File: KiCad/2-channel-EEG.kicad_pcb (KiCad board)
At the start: 4 copper layers, 90.4 x 55.9 mm, 79 parts, among them J1 Power_Input, J10 ADC_Data, J11 ISO_IN_C, J12 CH1_AVG_EN, J13 MCU_Data, J14 CH2_AVG_EN, J2 Nucleo_3.3, J3 Electrode_Input, J4 GND_select, J5 CH1_REF_Sel, J6 CH2_REF_Sel, J7 Conn_02x01, J8 Conn_02x01, J9 ADC_23, SW1 SW_Push_SPDT, U1 PESE1-S5-S5-M-TR, U10 AD8606, U11 ISO6763-Q1, U2 AD8237, U3 AD8237, U4 AD8606, U5 AD8606, U6 TCR2EF33, U7 AD8606, U8 AD8606, U9 MCP3562R

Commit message: PCB updates
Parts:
- removed J5: CH1_REF_Sel, Connector_PinHeader_2.54mm:PinHeader_2x02_P2.54mm_Vertical
- removed J6: CH2_REF_Sel, Connector_PinHeader_2.54mm:PinHeader_2x02_P2.54mm_Vertical
- U9: footprint Package_QFP:TQFP-52-1EP_10x10mm_P0.65mm_EP6.5x6.5mm -> Package_SO:TSSOP-20_4.4x6.5mm_P0.65mm
- moved J10 186.1 mm to (195.6, 102.6), turned to -90 degrees
- moved C19 179.7 mm to (186.7, 114.0), turned to -90 degrees
- moved C23 173.8 mm to (186.7, 107.7), turned to -90 degrees
- moved J9 169.2 mm to (200.4, 113.8), turned to 90 degrees
- moved U9 167.4 mm to (191.9, 112.0), turned to 90 degrees
- moved C24 165.4 mm to (184.4, 91.0), turned to 90 degrees
- moved C25 160.8 mm to (184.4, 82.8), turned to -90 degrees
- moved J13 160.2 mm to (179.6, 82.8), turned to -90 degrees
- moved J11 156.0 mm to (200.4, 102.6)
- moved J8 155.6 mm to (182.9, 114.3), turned to -90 degrees
- moved J7 154.6 mm to (182.9, 107.4), turned to -90 degrees
- moved C12 150.1 mm to (162.8, 86.6), turned to -90 degrees
- moved U11 147.8 mm to (191.3, 86.9), turned to 90 degrees
- moved C4 146.5 mm to (147.7, 98.6), turned to 90 degrees
- moved R11 136.8 mm to (162.6, 94.7), turned to -90 degrees
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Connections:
- C25 pad 1: +3.3V -> +3.3V_nucleo
- C4 pad 2: +3.3V -> +5V_iso
- C6 pad 1: /REF1_INT -> Net-(U2-VREF)
- C7 pad 1: /REF2_INT -> Net-(U3-VREF)
- C9 pad 2: +3.3V -> +5V_iso
- J10 pad 1: /ADC_SDO -> /ADC_~{CS}
- J10 pad 2: /ADC_SDI -> /ADC_SCK
- J10 pad 3: /ADC_SCK -> /ADC_SDI
- J10 pad 4: /ADC_~{CS} -> /ADC_SDO
- J10 pad 5: /ADC_MCLK -> /ADC_~{IRQ}
- J10 pad 6: /ADC_~{IRQ} -> /ADC_MCLK
- J2 pad 1: +3.3V -> +3.3V_nucleo
- J3 pad 1: /CH2+ -> /CH2-
- J3 pad 2: /CH2- -> /CH2+
- RN1 pad 3: /CH1- -> /CH1+
- RN1 pad 4: /CH1+ -> /CH1-
- RN2 pad 3: /CH2- -> /CH2+
- RN2 pad 4: /CH2+ -> /CH2-
- SW1 pad 1: +3.3V -> +5V_iso
- U1 pad 5: +3.3V -> +5V_iso
- U11 pad 16: +3.3V -> +3.3V_nucleo
- U2 pad 6: /CH1_REF -> Net-(U2-VREF)
- U3 pad 6: /CH2_REF -> Net-(U3-VREF)
- U4 pad 1: /REF1_INT -> Net-(U2-VREF)
- U5 pad 1: /REF2_INT -> Net-(U3-VREF)
- U6 pad 1: +3.3V -> +5V_iso
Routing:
- net +5V_iso: track 0.00 -> 24.2 mm
- net /ADC_SDO: track 0.00 -> 24.2 mm
- net GND1: track 0.00 -> 23.8 mm
- net /ADC_~{IRQ}: track 0.00 -> 21.9 mm
- net /ADC_~{CS}: track 0.00 -> 19.0 mm
- net /ADC_SDI: track 0.00 -> 18.9 mm
- net +3.3V: track 33.0 -> 51.7 mm, vias 13 -> 17
- net /ADC_SCK: track 0.00 -> 17.8 mm
- net GND: track 24.0 -> 40.2 mm, vias 15 -> 26
- net Net-(J12-Pin_1): track 0.00 -> 12.1 mm
- net +5V: track 0.00 -> 11.9 mm
- net /REF2_INT: track 11.3 -> 0.00 mm
- net /REF1_INT: track 11.2 -> 0.00 mm
- net /ADC0: track 0.00 -> 11.1 mm
- net Net-(U10A--): track 0.00 -> 11.1 mm
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- removed copper zone on F.Cu, net +3.3V
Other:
- board size 90.4 x 55.9 mm -> 270.1 x 148.1 mm
- board text added: "+"
- board text added: "+3.3V_NUCLEO"
- board text added: "-"
- board text added: "2-Channel EEG"
- board text added: "5V_in"
- board text added: "ADC2"
- board text added: "ADC3"
- board text added: "ADC_MCLK"
- board text added: "ADC_SCK"
- board text added: "ADC_SDI"
- board text added: "ADC_SDO"
- board text added: "ADC_~{CS}"
- board text added: "ADC_~{IRQ}"
- board text added: "CH1"
- board text added: "CH1+"
- board text added: "CH1-"
- board text added: "CH1_CM"
- board text added: "CH1_GAIN"
- board text added: "CH2"
- board text added: "CH2+"
- board text added: "CH2-"
- board text added: "CH2_CM"
- board text added: "CH2_GAIN"
- board text added: "CH_GND"
- board text added: "ISO_INC"
- board text added: "ISO_OUTC"
- board text added: "MCU_SCK"
- board text added: "MCU_SDI"
- board text added: "MCU_SDO"
- board text added: "MCU_~{CS}"
- board text added: "MCU_~{IRQ}"
- board text added: "OFF"
- board text added: "ON"
- board text added: "T.E"

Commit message: drl filter, additional caps for adc, Rs for adc spi.
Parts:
- removed the R20 at (143.0, 119.9)
- added C19: 10u, Capacitor_SMD:C_0805_2012Metric_Pad1.18x1.45mm_HandSolder, F.Cu at (192.5, 120.4)
- added C25: 10u, Capacitor_SMD:C_0805_2012Metric_Pad1.18x1.45mm_HandSolder, F.Cu at (186.4, 112.0)
- added C27: 1u, Capacitor_SMD:C_0805_2012Metric_Pad1.18x1.45mm_HandSolder, F.Cu at (166.3, 141.5)
- added R23: 10, Resistor_SMD:R_0805_2012Metric_Pad1.20x1.40mm_HandSolder, F.Cu at (186.2, 107.2)
- added R24: 10, Resistor_SMD:R_0805_2012Metric_Pad1.20x1.40mm_HandSolder, F.Cu at (188.5, 107.2)
- added R25: 10, Resistor_SMD:R_0805_2012Metric_Pad1.20x1.40mm_HandSolder, F.Cu at (190.8, 107.2)
- added R26: 10, Resistor_SMD:R_0805_2012Metric_Pad1.20x1.40mm_HandSolder, F.Cu at (193.0, 107.2)
- added R27: 10, Resistor_SMD:R_0805_2012Metric_Pad1.20x1.40mm_HandSolder, F.Cu at (195.3, 107.2)
- added R28: 10, Resistor_SMD:R_0805_2012Metric_Pad1.20x1.40mm_HandSolder, F.Cu at (197.6, 107.2)
- added R29: 1M, Resistor_SMD:R_0805_2012Metric_Pad1.20x1.40mm_HandSolder, F.Cu at (161.6, 144.2)
- C17: value C -> 10u
- C18: value 2u -> 10u
- C20: value 1u -> 10u
- R18: value R -> 100
- moved C20 38.8 mm to (186.4, 116.1), turned to -90 degrees
- moved C24 4.77 mm to (188.7, 112.0)
- moved J2 3.26 mm to (203.2, 92.7)
- moved C21 2.87 mm to (188.7, 116.1)
- moved U10 2.62 mm to (193.5, 114.0)
- renumbered C19 to C21, C21 to C22, C22 to C23, C23 to C24, C24 to C26, C25 to C28, J12 to J10, J13 to J11, J14 to J12, J7 to J5, J8 to J6, J9 to J7, J10 to J8, J11 to J9, R21 to R20, R22 to R21, R23 to R22, U9 to U10, U10 to U9
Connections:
- net +3.3V_nucleo renamed +3V3_nucleo
- C20 pad 1: /Driven_GND -> GND
- C20 pad 2: Net-(C20-Pad2) -> +3.3V
- C22 pad 1: Net-(C20-Pad2) -> /Driven_GND
- J10 pad 1: Net-(J12-Pin_1) -> Net-(J10-Pin_1)
- J12 pad 1: Net-(J12-Pin_1) -> Net-(J10-Pin_1)
- R20 pad 1: Net-(C20-Pad2) -> /Driven_GND
- R21 pad 1: Net-(C20-Pad2) -> /Driven_GND
- U10 pad 13: /ADC_~{CS} -> Net-(U10-~{CS})
- U10 pad 14: /ADC_SCK -> Net-(U10-SCK)
- U10 pad 15: /ADC_SDI -> Net-(U10-SDI)
- U10 pad 16: /ADC_SDO -> Net-(U10-SDO)
- U10 pad 17: /ADC_~{IRQ} -> Net-(U10-~{IRQ}/MDAT)
- U10 pad 18: /ADC_MCLK -> Net-(U10-MCLK)
- U10 pad 3: unconnected-(U9-REFIN--Pad3) -> GND
- U10 pad 4: unconnected-(U9-REFIN+/OUT-Pad4) -> Net-(U10-REFIN+/OUT)
- U9 pad 5: Net-(J12-Pin_1) -> Net-(U9B-+)
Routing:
- net Net-(J12-Pin_1): track 12.1 -> 0.00 mm
- net (no net): track 0.00 -> 12.1 mm
- net /ADC0: track 11.1 -> 0.00 mm
- net /ADC_MCLK: track 10.8 -> 0.00 mm
- net /ADC1: track 10.6 -> 0.00 mm
- net /ADC2: track 9.30 -> 0.00 mm
- net /ADC3: track 8.82 -> 0.00 mm
- net Net-(U10-MCLK): track 0.00 -> 7.57 mm
- net Net-(C20-Pad2): track 7.56 -> 0.00 mm
- net /Driven_GND: track 0.00 -> 7.56 mm
- net Net-(U10-~{IRQ}/MDAT): track 0.00 -> 5.78 mm
- net /ADC_~{IRQ}: track 21.9 -> 17.6 mm
- net Net-(U10-SDO): track 0.00 -> 4.26 mm
- net Net-(U10-~{CS}): track 0.00 -> 4.11 mm
- net Net-(U10-SDI): track 0.00 -> 3.34 mm
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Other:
- board size 270.1 x 148.1 mm -> 341.9 x 204 mm
- board text added: "V1.0"

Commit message: updated DRL and pcb
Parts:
- removed the J10 at (141.7, 104.1)
- removed J12: CH2_AVG_EN, Connector_PinHeader_2.54mm:PinHeader_2x01_P2.54mm_Vertical
- removed the R20 at (146.3, 108.2)
- added C26: 0.1u, Capacitor_SMD:C_0805_2012Metric_Pad1.18x1.45mm_HandSolder, F.Cu at (153.9, 107.4)
- added C29: 1u, Capacitor_SMD:C_0805_2012Metric_Pad1.18x1.45mm_HandSolder, F.Cu at (149.8, 111.7)
- added J7: VGND, Connector_PinHeader_2.54mm:PinHeader_1x01_P2.54mm_Vertical, F.Cu at (126.7, 115.8)
- added R22: 10k, Resistor_SMD:R_0805_2012Metric_Pad1.20x1.40mm_HandSolder, F.Cu at (143.8, 106.7)
- added R30: 1M, Resistor_SMD:R_0805_2012Metric_Pad1.20x1.40mm_HandSolder, F.Cu at (145.7, 111.7)
- added U11: AD8606, Package_SO:MSOP-8_3x3mm_P0.65mm, F.Cu at (148.3, 108.4)
- moved R29 45.5 mm to (149.6, 100.3), turned to 90 degrees
- moved C28 45.3 mm to (147.3, 100.3), turned to -90 degrees
- moved R20 12.1 mm to (138.2, 104.6), turned to 90 degrees
- moved C22 10.9 mm to (140.3, 104.6), turned to 90 degrees
- moved J3 10.2 mm to (126.7, 101.3), turned to 0 degrees
- moved R21 9.87 mm to (139.4, 101.3), turned to 0 degrees
- moved C23 9.12 mm to (139.4, 99.3), turned to 0 degrees
- moved J5 7.11 mm to (182.9, 114.6)
- moved U9 6.95 mm to (143.3, 101.3), turned to 90 degrees
- moved J6 6.87 mm to (182.9, 107.4)
- moved J4 6.27 mm to (140.0, 114.3), turned to 180 degrees
- moved J8 2.55 mm to (200.4, 111.2), turned to -90 degrees
- moved RN1 2.32 mm to (148.8, 104.4), turned to 180 degrees
- moved C4 2.05 mm to (149.1, 97.0), turned to 180 degrees
- moved C19 1.63 mm to (193.8, 119.4), turned to 0 degrees
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- renumbered C17 to C16, C18 to C17, C16 to C18, C3 to C2, C26 to C27, C27 to C28, C2 to C3, C28 to C30, C7 to C6, C6 to C7, J9 to J10, J7 to J8, J8 to J9, R3 to R1, R16 to R14, R17 to R15, R14 to R16, R15 to R17, R4 to R2, R21 to R20, R22 to R21, R1 to R3, R2 to R4, R6 to R5, R5 to R6, R8 to R7, R7 to R8, U11 to U12, U3 to U2, U2 to U3, U5 to U4, U4 to U5
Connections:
- C16 pad 2: /CH2_AO -> /CH1_AO
- C17 pad 2: /CH1_AO -> /CH2_AO
- C28 pad 2: Net-(J10-Pin_1) -> Net-(C28-Pad2)
- J3 pad 1: /CH2- -> /CH2+
- J3 pad 2: /CH2+ -> /CH2-
- J3 pad 4: /CH1- -> /CH1+
- J3 pad 5: /CH1+ -> /CH1-
- J4 pad 3: unconnected-(J4-Pin_3-Pad3) -> /VGND
- R18 pad 1: /CH2_AO -> /CH1_AO
- R19 pad 1: /CH1_AO -> /CH2_AO
- RN1 pad 1: Net-(J10-Pin_2) -> Net-(C28-Pad2)
- RN1 pad 2: Net-(J10-Pin_2) -> Net-(C28-Pad2)
- RN1 pad 3: /CH1+ -> /CH2+
- RN1 pad 4: /CH1- -> /CH2-
- RN2 pad 3: /CH2+ -> /CH1+
- RN2 pad 4: /CH2- -> /CH1-
- U2 pad 2: /CH2+ -> /CH1+
- U2 pad 3: /CH2- -> /CH1-
- U3 pad 2: /CH1+ -> /CH2+
- U3 pad 3: /CH1- -> /CH2-
- U9 pad 1: Net-(R20-Pad2) -> /Driven_GND
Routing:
- net /CH2+: track 3.71 -> 27.0 mm
- net /ISO_INC: track 0.18 -> 20.7 mm
- net /ADC1: track 0.00 -> 15.0 mm
- net (no net): track 12.1 -> 0.00 mm
- net /ADC0: track 0.00 -> 11.7 mm
- net /ADC2: track 0.00 -> 8.66 mm
- net /ADC3: track 0.00 -> 6.96 mm
- net Net-(U11A-+): track 0.00 -> 6.14 mm
- net Net-(U9B-+): track 0.00 -> 5.42 mm
- net /ADC_MCLK: track 0.00 -> 4.94 mm
- net Net-(J10-Pin_2): track 4.23 -> 0.00 mm
- net Net-(U9A--): track 11.1 -> 7.12 mm
- net Net-(U11A--): track 0.00 -> 3.22 mm
- net Net-(C28-Pad2): track 0.00 -> 2.80 mm
- net GND: track 40.4 -> 37.7 mm, vias 23 -> 21
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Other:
- board text removed: "CH1_CM"
- board text removed: "CH2_CM"
- board text removed: "CH2_GAIN"

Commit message: added solder jumpers between INA and filter
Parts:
- added JP1: SolderJumper_2_Open, Resistor_SMD:R_0603_1608Metric, F.Cu at (158.5, 109.3)
- added JP2: SolderJumper_2_Open, Resistor_SMD:R_0603_1608Metric, F.Cu at (158.5, 99.1)
- moved J4 5.36 mm to (137.2, 109.7), turned to 0 degrees
- moved J10 3.78 mm to (203.2, 105.2)
- moved J8 2.79 mm to (203.2, 111.2)
- moved C4 2.15 mm to (147.1, 96.3), turned to 90 degrees
- moved U1 1.90 mm to (141.0, 89.4)
- moved RV2 1.80 mm to (170.2, 95.5)
- moved R11 1.72 mm to (164.1, 94.0), turned to 0 degrees
- moved R21 1.70 mm to (137.9, 100.6), turned to 90 degrees
- moved C23 1.54 mm to (140.3, 100.6), turned to 90 degrees
- moved R7 1.52 mm to (158.5, 107.4)
- moved C19 1.52 mm to (192.3, 119.4), turned to 180 degrees
- moved J3 1.52 mm to (126.7, 99.8)
- moved R8 1.52 mm to (158.5, 97.0)
- moved R17 1.30 mm to (177.5, 99.1)
- moved J11 1.27 mm to (179.6, 84.1)
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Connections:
- R1 pad 1: Net-(R1-Pad1) -> Net-(JP1-A)
- R21 pad 1: Net-(U9A--) -> Net-(U9B--)
- R21 pad 2: Net-(U9B--) -> Net-(U9A--)
- R3 pad 1: Net-(R3-Pad1) -> Net-(JP2-A)
- R5 pad 2: Net-(R1-Pad1) -> Net-(JP1-A)
- R6 pad 2: Net-(R3-Pad1) -> Net-(JP2-A)
- R7 pad 2: Net-(R1-Pad1) -> Net-(JP1-B)
- R8 pad 2: Net-(R3-Pad1) -> Net-(JP2-B)
- U2 pad 8: Net-(R1-Pad1) -> Net-(JP1-A)
- U3 pad 8: Net-(R3-Pad1) -> Net-(JP2-A)
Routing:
- net GND1: track 23.8 -> 88.5 mm, vias 0 -> 2
- net /MCU_~{CS}: track 0.00 -> 31.6 mm
- net /MCU_SCK: track 0.00 -> 27.3 mm
- net /CH2-: track 2.14 -> 27.3 mm, vias 0 -> 2
- net +3.3V: track 49.6 -> 74.0 mm, vias 13 -> 26
- net /CH1-: track 2.44 -> 26.5 mm
- net /CH1+: track 3.71 -> 27.1 mm
- net GND: track 37.7 -> 61.0 mm, vias 21 -> 37
- net +3V3_nucleo: track 2.60 -> 25.8 mm, vias 0 -> 2
- net /MCU_SDI: track 0.00 -> 23.1 mm
- net /ISO_OUTC: track 0.00 -> 19.1 mm
- net /CH_GND: track 0.00 -> 16.0 mm
- net /MCU_~{IRQ}: track 0.00 -> 15.2 mm
- net /MCU_SDO: track 0.00 -> 10.4 mm
- net Net-(JP1-A): track 0.00 -> 7.82 mm
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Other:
- board size 341.9 x 204 mm -> 84.1 x 43.9 mm
- board text added: "3.3V_MCU"
- board text added: "4/7/2024"
- board text added: "CH2_GAIN"
- board text added: "JLCJLCJLCJLC"
- board text added: "Tim Erwin"
- board text added: "VGND"
- board text removed: "+3.3V_NUCLEO"
- board text removed: "T.E"

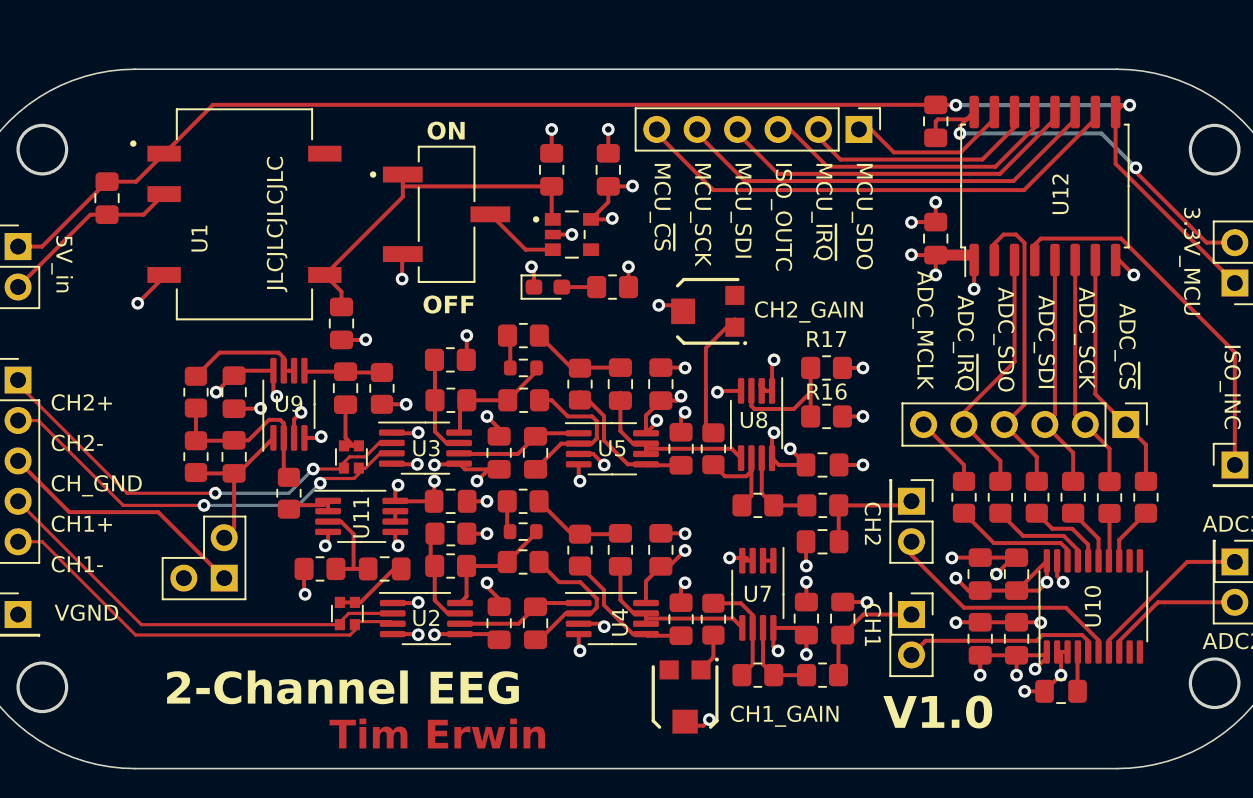
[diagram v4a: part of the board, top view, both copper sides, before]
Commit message: fix wrong reference C,R values
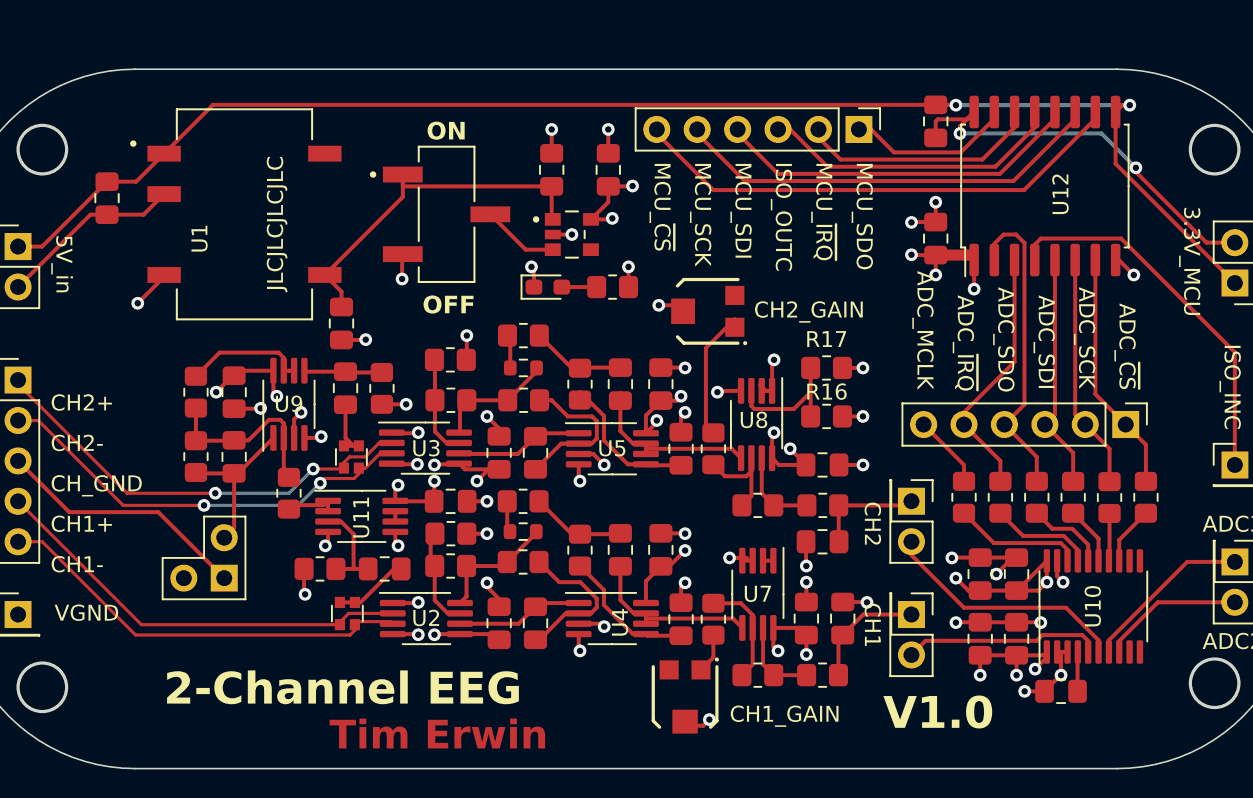
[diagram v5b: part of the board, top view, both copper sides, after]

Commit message: schematic BOM
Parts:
- turned R21 to -90 degrees
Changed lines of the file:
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@@
     )
     (pad_to_mask_clearance 0)
+    (aux_axis_origin 130.302 145.796)
     (pcbplotparams
       (layerselection 0x00010fc_ffffffff)
@@
     (property "ki_keywords" "dual opamp")
     (attr smd)
-    (fp_text reference "U11" (at 0 0.071 90) (layer "F.SilkS")
+    (fp_text reference "U11" (at 0 0.071 90) (layer "F.SilkS") hide
         (effects (font (size 1 1) (thickness 0.15)))
     )
@@
         (effects (font (size 1 1) (thickness 0.15)))
     )
-    (fp_text user "${REFERENCE}" (at -1.5 0.375 90) (layer "F.Fab")
+    (fp_text user "${REFERENCE}" (at 0 0.071 90) (layer "F.Fab")
         (effects (font (size 0.75 0.75) (thickness 0.11)))
     )
@@
     (property "ki_keywords" "instrumentation amplifier")
     (attr smd)
-    (fp_text reference "U2" (at 0 0 180) (layer "F.SilkS")
+    (fp_text reference "U2" (at 0 0 180) (layer "F.SilkS") hide
         (effects (font (size 1 1) (thickness 0.15)))
     )
@@
   )
   (footprint "Resistor_SMD:R_0805_2012Metric_Pad1.20x1.40mm_HandSolder" (layer "F.Cu")
-    (at 137.922 100.584 90)
+    (at 137.922 100.584 -90)
     (descr "Resistor SMD 0805 (2012 Metric), square (rectangular) end terminal, IPC_7351 nominal with elongated pad for handsoldering. (Body size source: IPC-SM-782 page 72, https://www.pcb-3d.com/wordpress/wp-content/uploads/ipc-sm-782a_amendment_1_and_2.pdf), generated with kicad-footprint-generator")
     (tags "resistor handsolder")
@@
     (fp_line (start 1 0.625) (end -1 0.625)
       (stroke (width 0.1) (type solid)) (layer "F.Fab"))
-    (pad "1" smd roundrect (at -1 0 90) (size 1.2 1.4) (layers "F.Cu" "F.Paste" "F.Mask") (roundrect_rratio 0.2083333333)
+    (pad "1" smd roundrect (at -1 0 270) (size 1.2 1.4) (layers "F.Cu" "F.Paste" "F.Mask") (roundrect_rratio 0.2083333333)
       (net 53 "Net-(U9B--)") (pintype "passive"))
-    (pad "2" smd roundrect (at 1 0 90) (size 1.2 1.4) (layers "F.Cu" "F.Paste" "F.Mask") (roundrect_rratio 0.2083333333)
+    (pad "2" smd roundrect (at 1 0 270) (size 1.2 1.4) (layers "F.Cu" "F.Paste" "F.Mask") (roundrect_rratio 0.2083333333)
       (net 42 "Net-(U9A--)") (pintype "passive"))
     (model "${KICAD6_3DMODEL_DIR}/Resistor_SMD.3dshapes/R_0805_2012Metric.wrl"
@@
         (effects (font (size 1 1) (thickness 0.15)))
     )
-    (fp_text user "${REFERENCE}" (at 1.524 -1.016) (layer "F.Fab")
+    (fp_text user "${REFERENCE}" (at -0.016 0) (layer "F.Fab")
         (effects (font (size 0.4 0.4) (thickness 0.06)))
     )
@@
     (property "ki_keywords" "dual opamp")
     (attr smd)
-    (fp_text reference "U9" (at 0 0 180) (layer "F.SilkS")
+    (fp_text reference "U9" (at 0 0 180) (layer "F.SilkS") hide
         (effects (font (size 1 1) (thickness 0.15)))
     )

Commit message: final edits before ordering PCB
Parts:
- added R20: 0, Resistor_SMD:R_0805_2012Metric_Pad1.20x1.40mm_HandSolder, F.Cu at (140.5, 104.6)
- C10, C11: value 100n -> 0.1u
- C13, C14: value 50n -> 47n
- C5: renamed from C6; value 3.3u -> 10u
- C6: renamed from C7; value 3.3u -> 10u
- J8: value ADC_23 -> Conn_01x03; footprint Connector_PinHeader_2.54mm:PinHeader_2x01_P2.54mm_Vertical -> Connector_PinHeader_2.54mm:PinHeader_1x03_P2.54mm_Vertical
- R10, R7, R8, R9: value 56k -> 56.2k
- R11: value 10k -> 510
- R5, R6: value 2M -> 3M
- moved J10 4.57 mm to (203.2, 100.6)
- moved J8 3.04 mm to (203.2, 108.2), turned to 0 degrees
- moved C22 2.40 mm to (137.9, 104.6)
- moved R21 2.03 mm to (135.9, 104.6)
- renumbered C8 to C7, C5 to C8, R20 to R21, R21 to R22, R22 to R23, R23 to R24, R24 to R25, R25 to R26, R26 to R27, R27 to R28, R28 to R29, R29 to R30, R30 to R31
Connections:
- J8 pad 1: /ADC2 -> /VGND
- U9 pad 1: /Driven_GND -> Net-(R20-Pad2)
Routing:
- net /ISO_INC: track 23.9 -> 19.0 mm
- net Net-(R20-Pad2): track 0.00 -> 2.40 mm
- net Net-(U9A--): track 11.5 -> 13.0 mm
- net /ADC3: track 8.96 -> 10.3 mm
- net /Driven_GND: track 10.1 -> 9.02 mm
- net GND: track 61.0 -> 60.6 mm, vias 37 -> 38
- net +3.3V: track 74.0 -> 74.2 mm, vias 26 -> 27
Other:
- board text added: "2"
- board text added: "3"
- board text added: "ISO_C"
- board text removed: "ADC2"
- board text removed: "ADC3"
- board text removed: "ISO_INC"
